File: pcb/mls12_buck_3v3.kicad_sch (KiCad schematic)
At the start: 12 parts, among them U2 LMR51606XDBVR

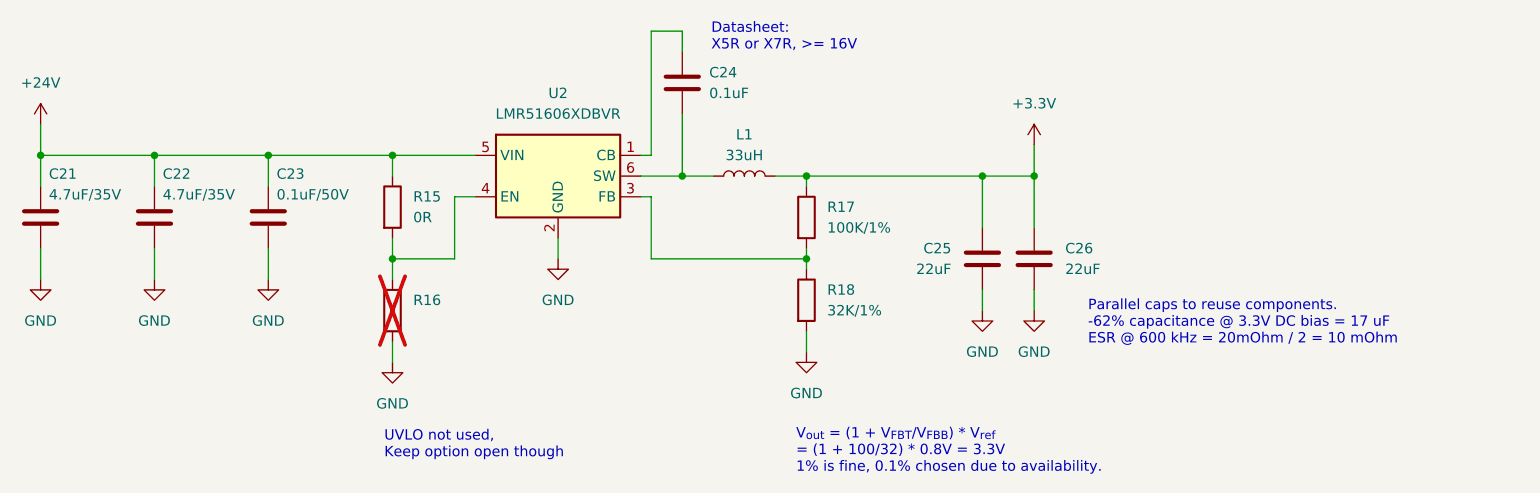
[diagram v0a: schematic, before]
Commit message: Update to 25W PoE+ module, 2 outputs
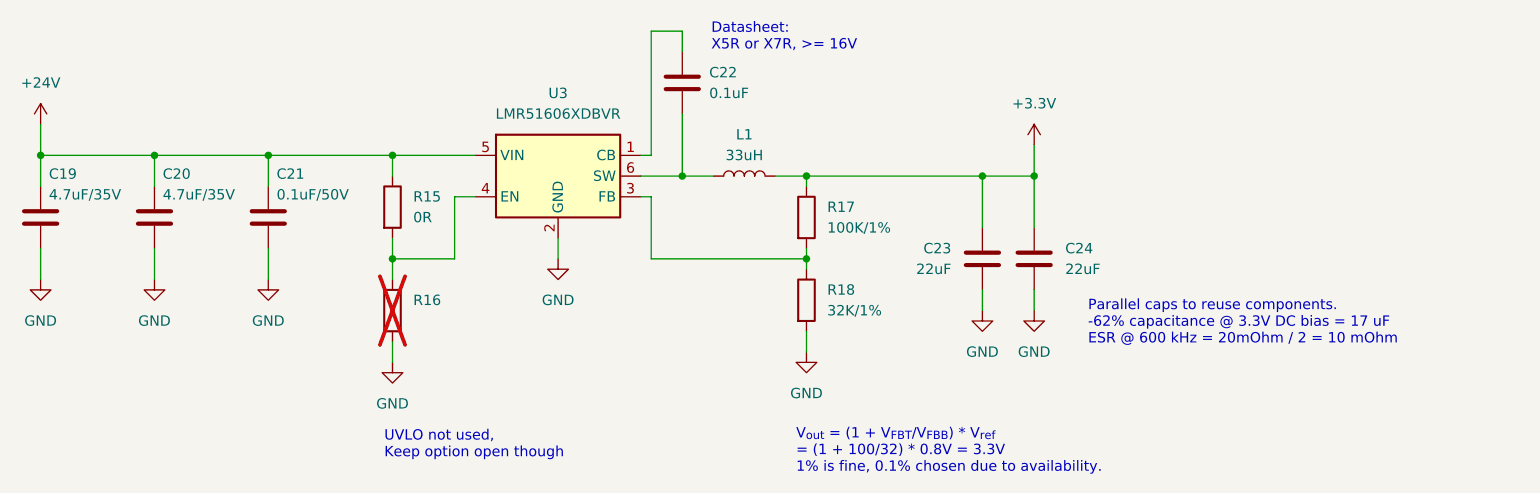
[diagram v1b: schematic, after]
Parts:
- renumbered C21 to C19, C22 to C20, C23 to C21, C24 to C22, C25 to C23, C26 to C24, U2 to U3
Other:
- company: (none) -> Quomodo BV

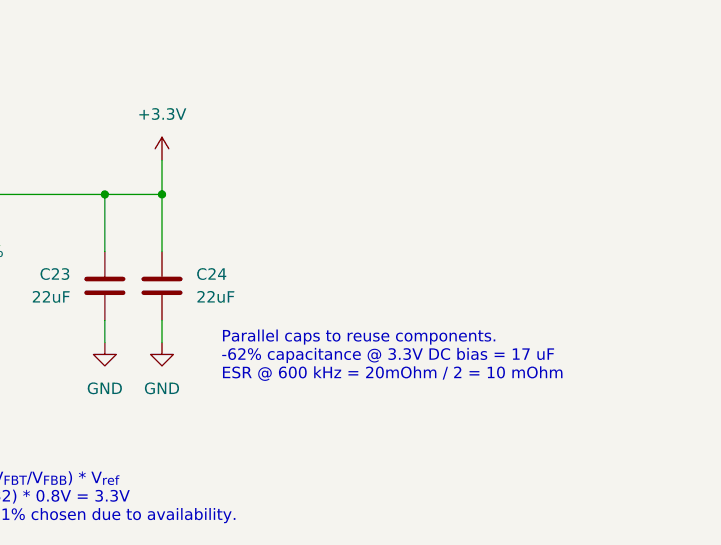
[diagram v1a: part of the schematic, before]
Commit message: Add test points
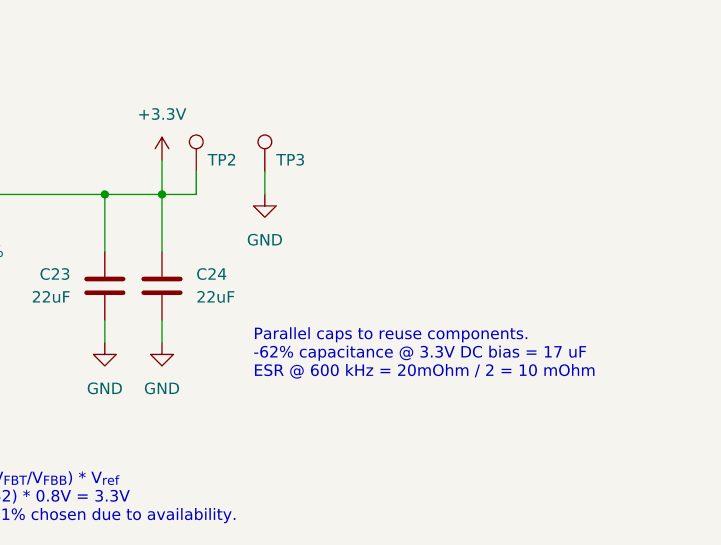
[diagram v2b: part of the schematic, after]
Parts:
- added TP2: TestPoint, TestPoint:TestPoint_Pad_D1.5mm, symbol Connector:TestPoint
- added TP3: TestPoint, TestPoint:TestPoint_Pad_1.5x1.5mm, symbol Connector:TestPoint
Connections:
- net +3.3V: now also TP2.1
- net GND: now also TP3.1
